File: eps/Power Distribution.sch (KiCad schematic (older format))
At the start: 44 parts, among them Q1 2N7002, Q10 IRF7404, Q11 IRF7404, Q12 2N7002, Q13 IRF7404, Q14 IRF7404, Q15 2N7002, Q16 IRF7404, Q17 IRF7404, Q2 2N7002, Q3 IRF7404, Q4 IRF7404, Q5 2N7002, Q6 2N7002, Q7 IRF7404, Q8 IRF7404, Q9 2N7002

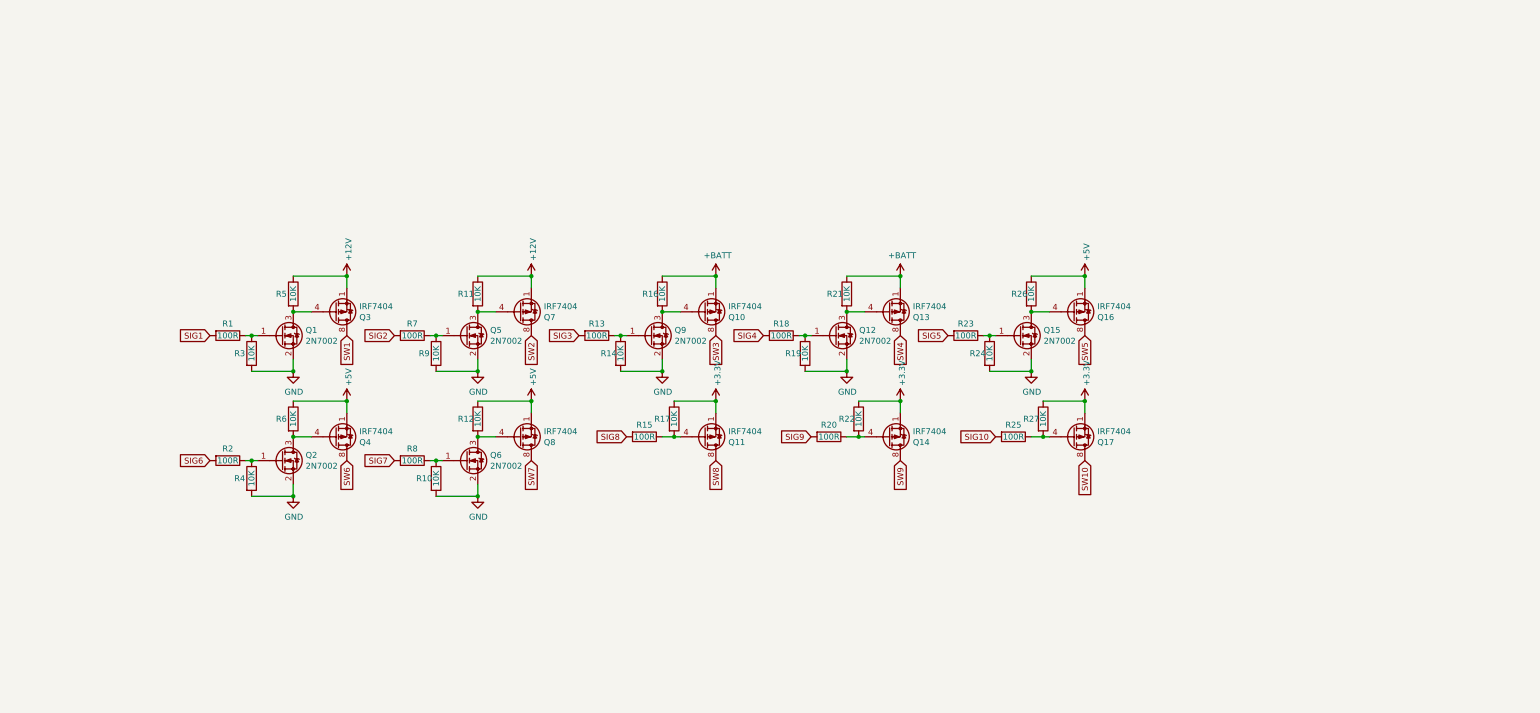
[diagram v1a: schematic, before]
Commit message: add analog mux for current sense
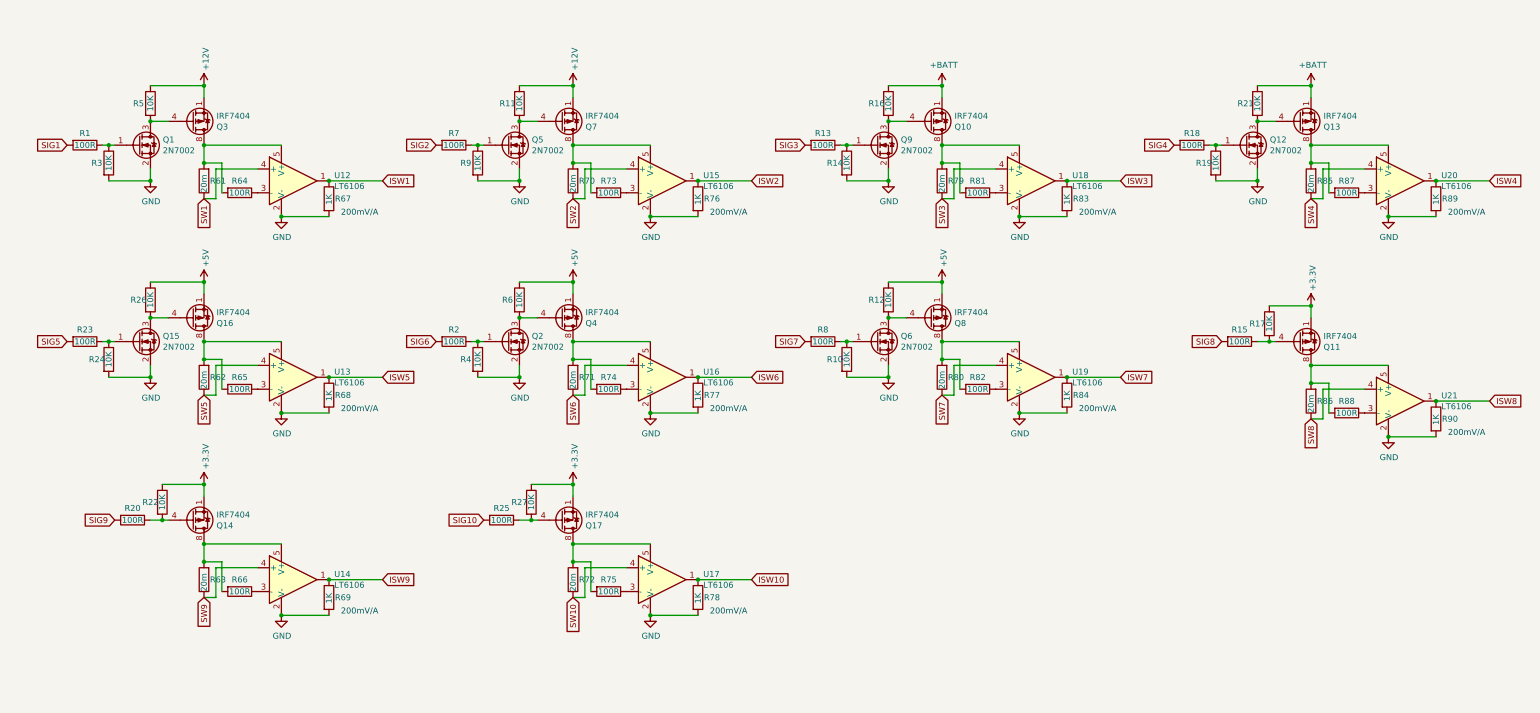
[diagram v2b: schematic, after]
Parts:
- added R61, R62, R63, R70, R71, R72, R79, R80, R85, R86: 20m, symbol Device:R
- added R64, R65, R66, R73, R74, R75, R81, R82, R87, R88: 100R, symbol Device:R
- added R67, R68, R69, R76, R77, R78, R83, R84, R89, R90: 1K, symbol Device:R
- added U12, U13, U14, U15, U16, U17, U18, U19, U20, U21: LT6106, Package_TO_SOT_SMD:SOT-23-5, symbol Amplifier_Current:LT6106
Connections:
- net GND: now also R67.2, R68.2, R69.2, R76.2, R77.2, R78.2, R83.2, R84.2, R89.2, R90.2, U12.2 (V-), U13.2 (V-), U14.2 (V-), U15.2 (V-), U16.2 (V-), U17.2 (V-), U18.2 (V-), U19.2 (V-), U20.2 (V-), U21.2 (V-)
- net SW1: now also R61.1, U12.4 (+); no longer Q3.5 (D), Q3.6 (D), Q3.7 (D), Q3.8 (D)
- net SW10: now also R72.1, U17.4 (+); no longer Q17.5 (D), Q17.6 (D), Q17.7 (D), Q17.8 (D)
- net SW2: now also R70.1, U15.4 (+); no longer Q7.5 (D), Q7.6 (D), Q7.7 (D), Q7.8 (D)
- net SW3: now also R79.1, U18.4 (+); no longer Q10.5 (D), Q10.6 (D), Q10.7 (D), Q10.8 (D)
- net SW4: now also R85.1, U20.4 (+); no longer Q13.5 (D), Q13.6 (D), Q13.7 (D), Q13.8 (D)
- net SW5: now also R62.1, U13.4 (+); no longer Q16.5 (D), Q16.6 (D), Q16.7 (D), Q16.8 (D)
- net SW6: now also R71.1, U16.4 (+); no longer Q4.5 (D), Q4.6 (D), Q4.7 (D), Q4.8 (D)
- net SW7: now also R80.1, U19.4 (+); no longer Q8.5 (D), Q8.6 (D), Q8.7 (D), Q8.8 (D)
- net SW8: now also R86.1, U21.4 (+); no longer Q11.5 (D), Q11.6 (D), Q11.7 (D), Q11.8 (D)
- net SW9: now also R63.1, U14.4 (+); no longer Q14.5 (D), Q14.6 (D), Q14.7 (D), Q14.8 (D)
- new net: Q3.5 (D), Q3.6 (D), Q3.7 (D), Q3.8 (D), R61.2, R64.2, U12.5 (V+)
- new net: R64.1, U12.3 (-)
- new net: Q7.5 (D), Q7.6 (D), Q7.7 (D), Q7.8 (D), R70.2, R73.2, U15.5 (V+)
- new net: R73.1, U15.3 (-)
- new net: Q10.5 (D), Q10.6 (D), Q10.7 (D), Q10.8 (D), R79.2, R81.2, U18.5 (V+)
- new net: R81.1, U18.3 (-)
- new net: Q13.5 (D), Q13.6 (D), Q13.7 (D), Q13.8 (D), R85.2, R87.2, U20.5 (V+)
- new net: R87.1, U20.3 (-)
- new net: Q16.5 (D), Q16.6 (D), Q16.7 (D), Q16.8 (D), R62.2, R65.2, U13.5 (V+)
- new net: R65.1, U13.3 (-)
- new net: Q4.5 (D), Q4.6 (D), Q4.7 (D), Q4.8 (D), R71.2, R74.2, U16.5 (V+)
- new net: R74.1, U16.3 (-)
- new net: Q8.5 (D), Q8.6 (D), Q8.7 (D), Q8.8 (D), R80.2, R82.2, U19.5 (V+)
- new net: R82.1, U19.3 (-)
- new net: Q11.5 (D), Q11.6 (D), Q11.7 (D), Q11.8 (D), R86.2, R88.2, U21.5 (V+)
- new net: R88.1, U21.3 (-)
- new net: Q14.5 (D), Q14.6 (D), Q14.7 (D), Q14.8 (D), R63.2, R66.2, U14.5 (V+)
- new net: R66.1, U14.3 (-)
- new net: Q17.5 (D), Q17.6 (D), Q17.7 (D), Q17.8 (D), R72.2, R75.2, U17.5 (V+)
- new net: R75.1, U17.3 (-)
- new net ISW1: R67.1, U12.1
- new net ISW10: R78.1, U17.1
- new net ISW2: R76.1, U15.1
- new net ISW3: R83.1, U18.1
- new net ISW4: R89.1, U20.1
- new net ISW5: R68.1, U13.1
- new net ISW6: R77.1, U16.1
- new net ISW7: R84.1, U19.1
- new net ISW8: R90.1, U21.1
- new net ISW9: R69.1, U14.1
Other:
- note added: "200mV/A\n"
- moved on the sheet: Q1, Q10, Q11, Q12, Q13, Q14, Q15, Q16, Q17, Q2, Q3, Q4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

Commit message: modify mux, implement hw watchdog, standardize p channel mosfets to irf7425
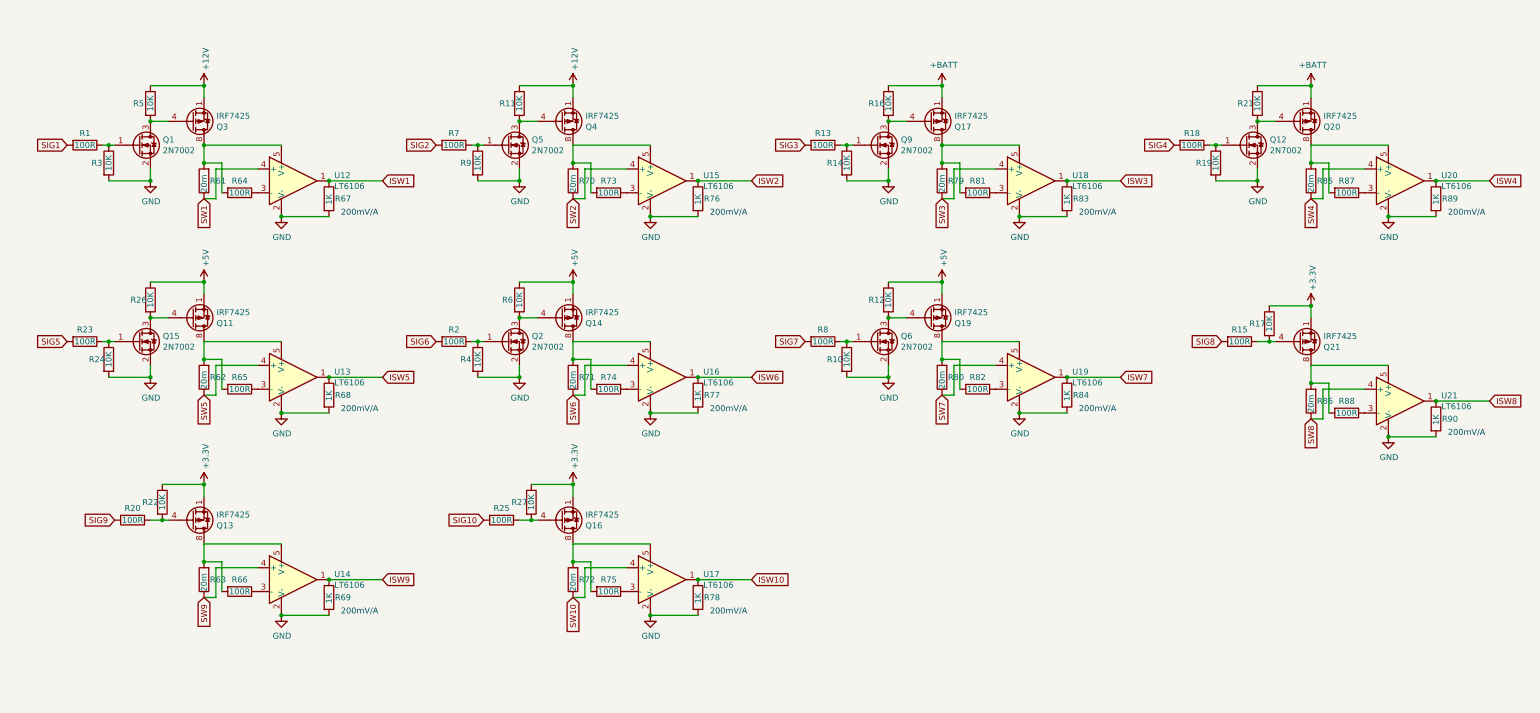
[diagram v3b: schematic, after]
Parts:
- removed Q10, Q7, Q8: IRF7404, Package_SO:SOIC-8_3.9x4.9mm_P1.27mm, symbol Transistor_FET:IRF7404
- added Q19, Q20, Q21: IRF7425, Package_SO:SOIC-8_3.9x4.9mm_P1.27mm, symbol Transistor_FET:IRF7404
- Q11, Q13, Q14, Q16, Q17, Q3, Q4: value IRF7404 -> IRF7425
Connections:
- net +12V: now also Q4.1 (S), Q4.2 (S), Q4.3 (S)
- net +3V3: now also Q13.1 (S), Q13.2 (S), Q13.3 (S), Q16.1 (S), Q16.2 (S), Q16.3 (S), Q21.1 (S), Q21.2 (S), Q21.3 (S); no longer Q11.1 (S), Q11.2 (S), Q11.3 (S), Q14.1 (S), Q14.2 (S), Q14.3 (S), Q17.1 (S), Q17.2 (S), Q17.3 (S)
- net +5V: now also Q11.1 (S), Q11.2 (S), Q11.3 (S), Q14.1 (S), Q14.2 (S), Q14.3 (S), Q19.1 (S), Q19.2 (S), Q19.3 (S); no longer Q16.1 (S), Q16.2 (S), Q16.3 (S), Q4.1 (S), Q4.2 (S), Q4.3 (S)
- net +BATT: now also Q17.1 (S), Q17.2 (S), Q17.3 (S), Q20.1 (S), Q20.2 (S), Q20.3 (S); no longer Q13.1 (S), Q13.2 (S), Q13.3 (S)
- net at R70.2, R73.2, U15.5 (V+): now also Q4.5 (D), Q4.6 (D), Q4.7 (D), Q4.8 (D)
- net at R79.2, R81.2, U18.5 (V+): now also Q17.5 (D), Q17.6 (D), Q17.7 (D), Q17.8 (D)
- net at Q13.5 (D), Q13.6 (D), Q13.7 (D)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: now also R63.2, R66.2, U14.5 (V+); no longer R85.2, R87.2, U20.5 (V+)
- net at Q16.5 (D), Q16.6 (D), Q16.7 (D)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: now also R72.2, R75.2, U17.5 (V+); no longer R62.2, R65.2, U13.5 (V+)
- net at R80.2, R82.2, U19.5 (V+): now also Q19.5 (D), Q19.6 (D), Q19.7 (D), Q19.8 (D)
- net at Q11.5 (D), Q11.6 (D), Q11.7 (D)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: now also R62.2, R65.2, U13.5 (V+); no longer R86.2, R88.2, U21.5 (V+)
- net at Q14.5 (D), Q14.6 (D), Q14.7 (D)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: now also R71.2, R74.2, U16.5 (V+); no longer R63.2, R66.2, U14.5 (V+)
- net at Q5.3 (D), R11.2: now also Q4.4 (G)
- net at Q9.3 (D), R16.2: now also Q17.4 (G)
- net at Q12.3 (D), R21.2: now also Q20.4 (G); no longer Q13.4 (G)
- net at Q15.3 (D), R26.2: now also Q11.4 (G); no longer Q16.4 (G)
- net at Q2.3 (D), R6.2: now also Q14.4 (G); no longer Q4.4 (G)
- net at Q6.3 (D), R12.2: now also Q19.4 (G)
- net at R15.1, R17.2: now also Q21.4 (G); no longer Q11.4 (G)
- net at R20.1, R22.2: now also Q13.4 (G); no longer Q14.4 (G)
- net at R25.1, R27.2: now also Q16.4 (G); no longer Q17.4 (G)
- new net: Q20.5 (D), Q20.6 (D), Q20.7 (D), Q20.8 (D), R85.2, R87.2, U20.5 (V+)
- new net: Q21.5 (D), Q21.6 (D), Q21.7 (D), Q21.8 (D), R86.2, R88.2, U21.5 (V+)

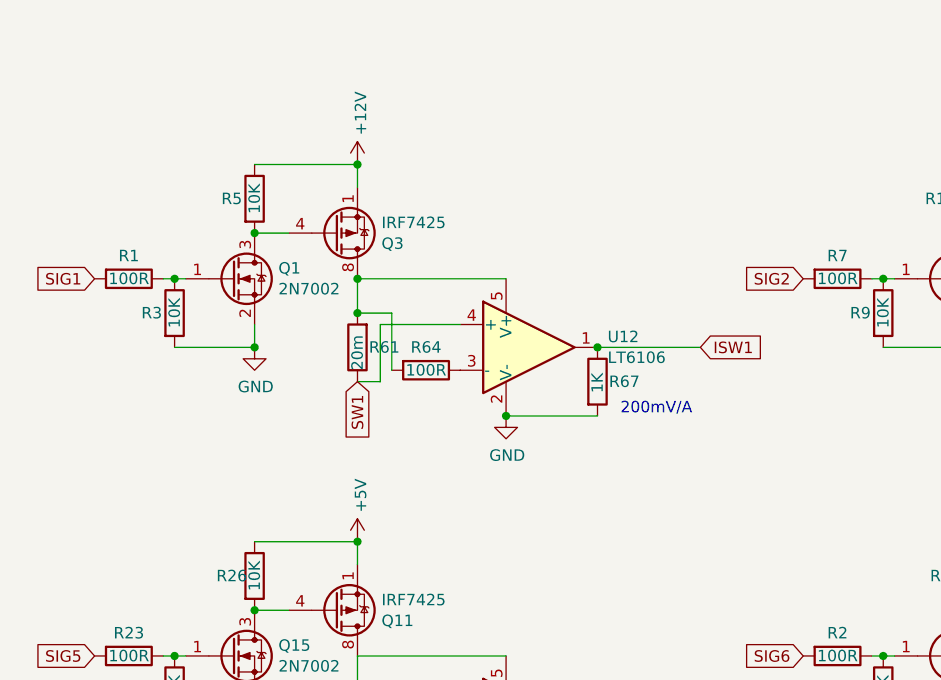
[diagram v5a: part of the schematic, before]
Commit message: start on adding LCLs to PDMs
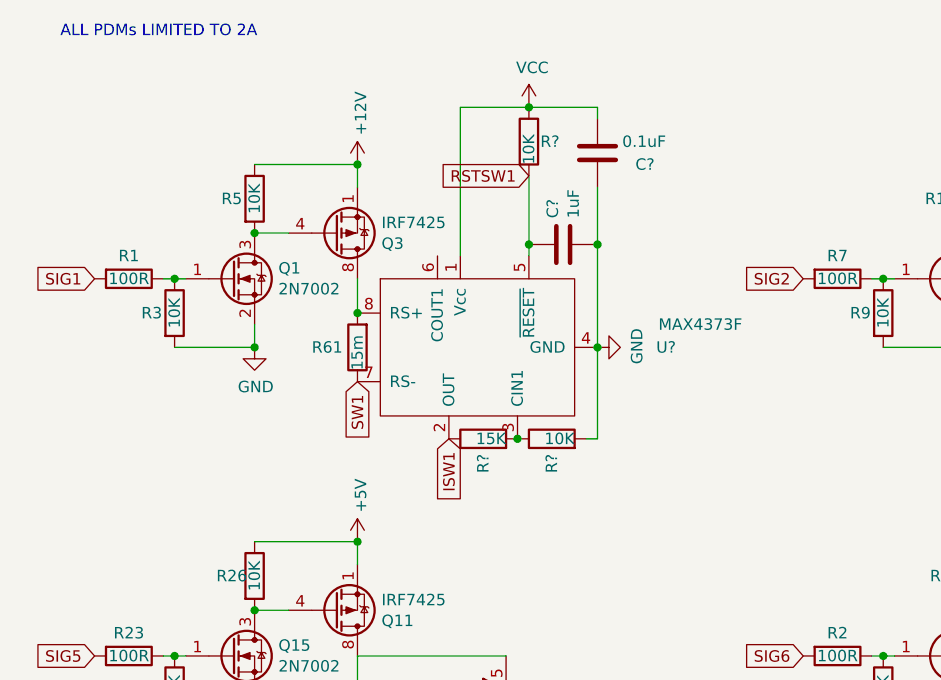
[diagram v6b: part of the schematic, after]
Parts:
- removed R64: 100R, symbol Device:R
- removed R67: 1K, symbol Device:R
- removed U12: LT6106, Package_TO_SOT_SMD:SOT-23-5, symbol Amplifier_Current:LT6106
- added C?: 0.1uF, symbol Device:C
- added C?: 1uF, symbol Device:C
- added R? (x2): 10K, symbol Device:R
- added R?: 15K, symbol Device:R
- added U?: MAX4373F, symbol epslib:MAX4373
- R61: value 20m -> 15m
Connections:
- net GND: now also C?.1, C?.2, R?.2, U?.4 (GND)
- net ISW1: now also R?.1, U?.2 (OUT)
- net SW1: now also U?.7 (RS-)
- net at Q3.5 (D), Q3.6 (D), Q3.7 (D)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: now also U?.8 (RS+)
- new net: R?.1, R?.2, U?.3 (CIN1)
- new net RSTSW1: C?.1, R?.2, U?.5 (~RESET)
- new net VCC: C?.2, R?.1, U?.1 (Vcc)
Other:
- note added: "ALL PDMs LIMITED TO 2A"
